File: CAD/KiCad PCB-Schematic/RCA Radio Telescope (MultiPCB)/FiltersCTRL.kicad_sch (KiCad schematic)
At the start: 12 parts, among them J11 Conn_01x04_MountingPin, U5 SN74AVC2T45DCUR, U6 MIC5365-1.8YC5-TR, U7 MIC5365-3.3YC5-TR

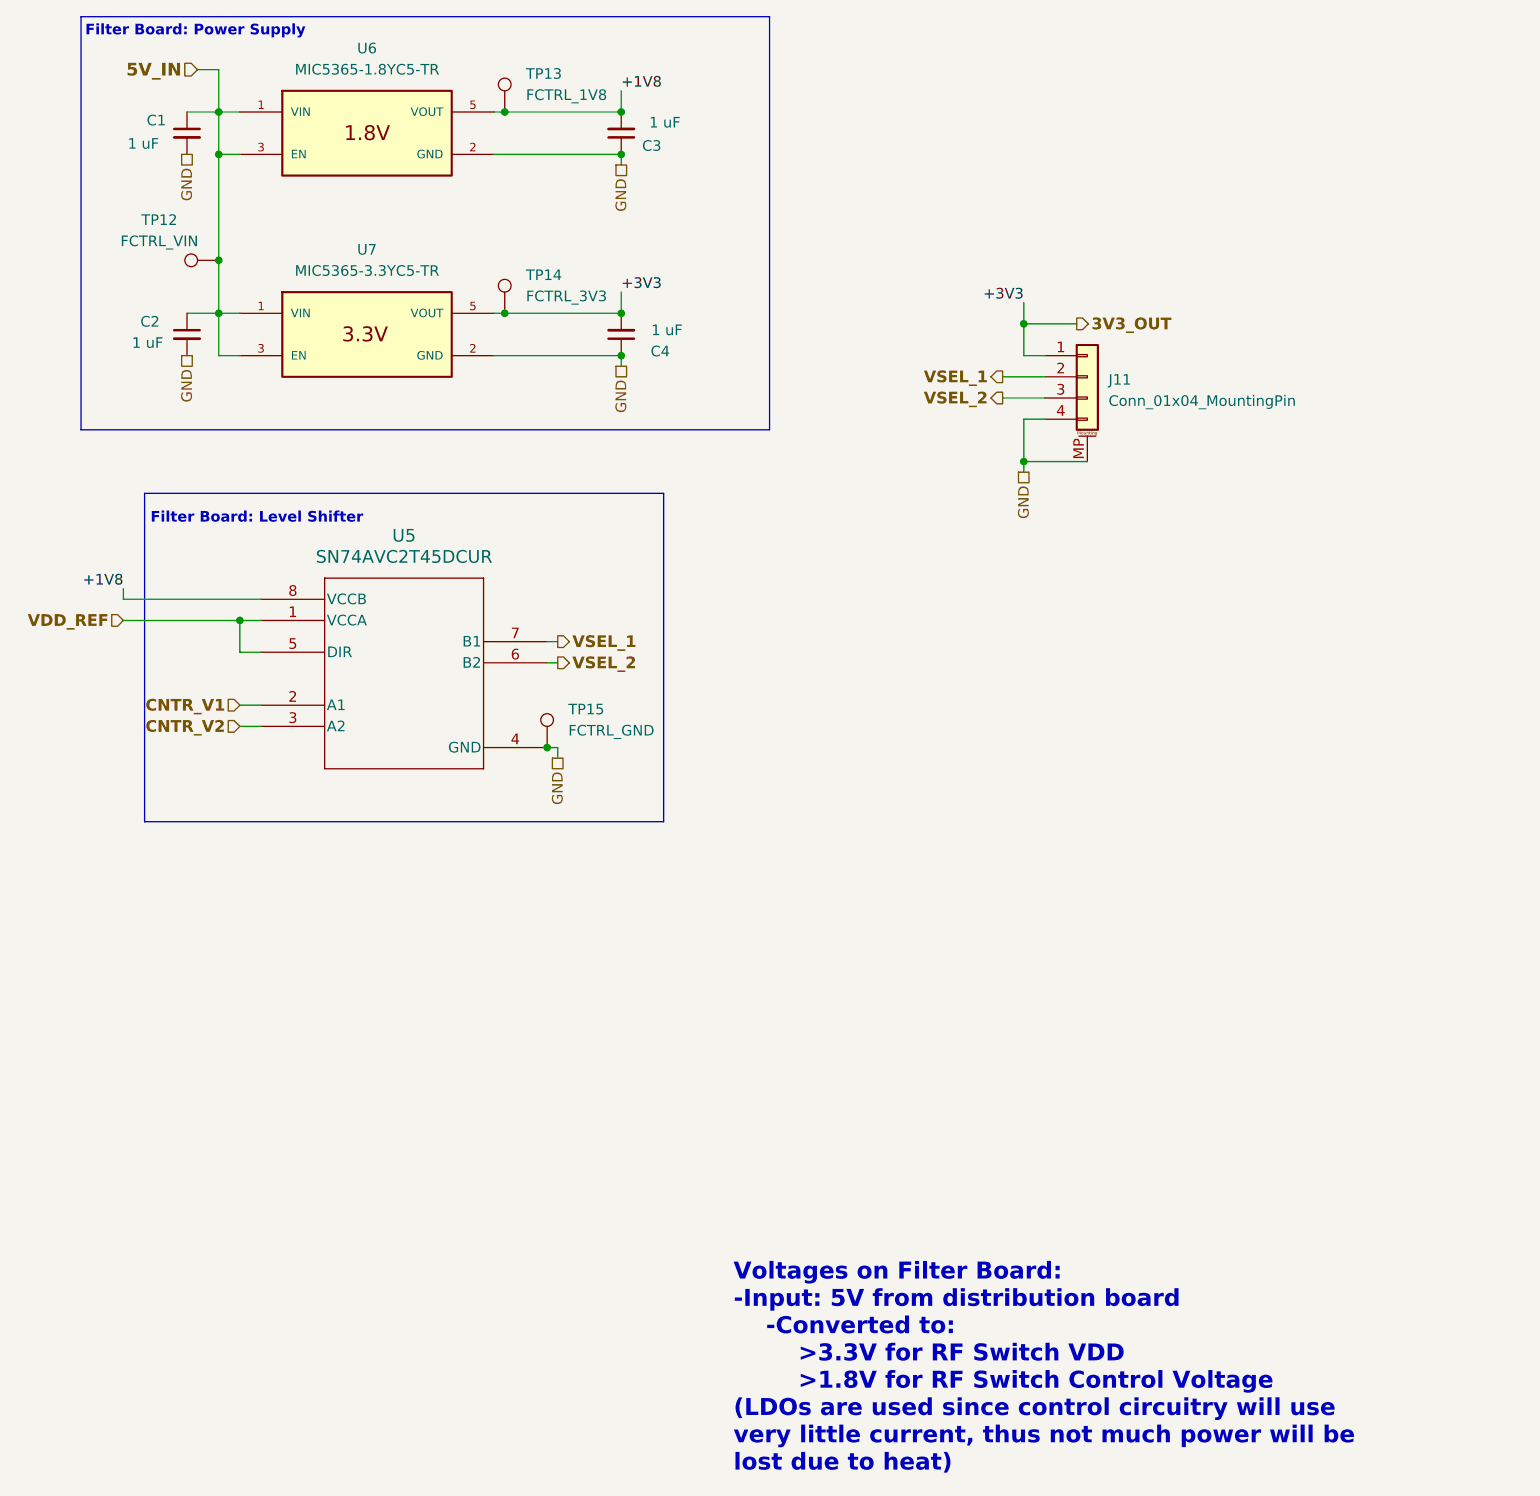
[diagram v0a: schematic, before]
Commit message: Update to Schematic and PCB
Filter Control Schematic to v1.5
- Removed redundant connector symbol

Root Schematic to v1.9
- Adjusted pin connections for J14 and J14

Created Matching Network PCB
- Filter Board Schematic renamed to MatchNetwork
- Placed RF switches, traces, holes for daughter board, and ground stitching
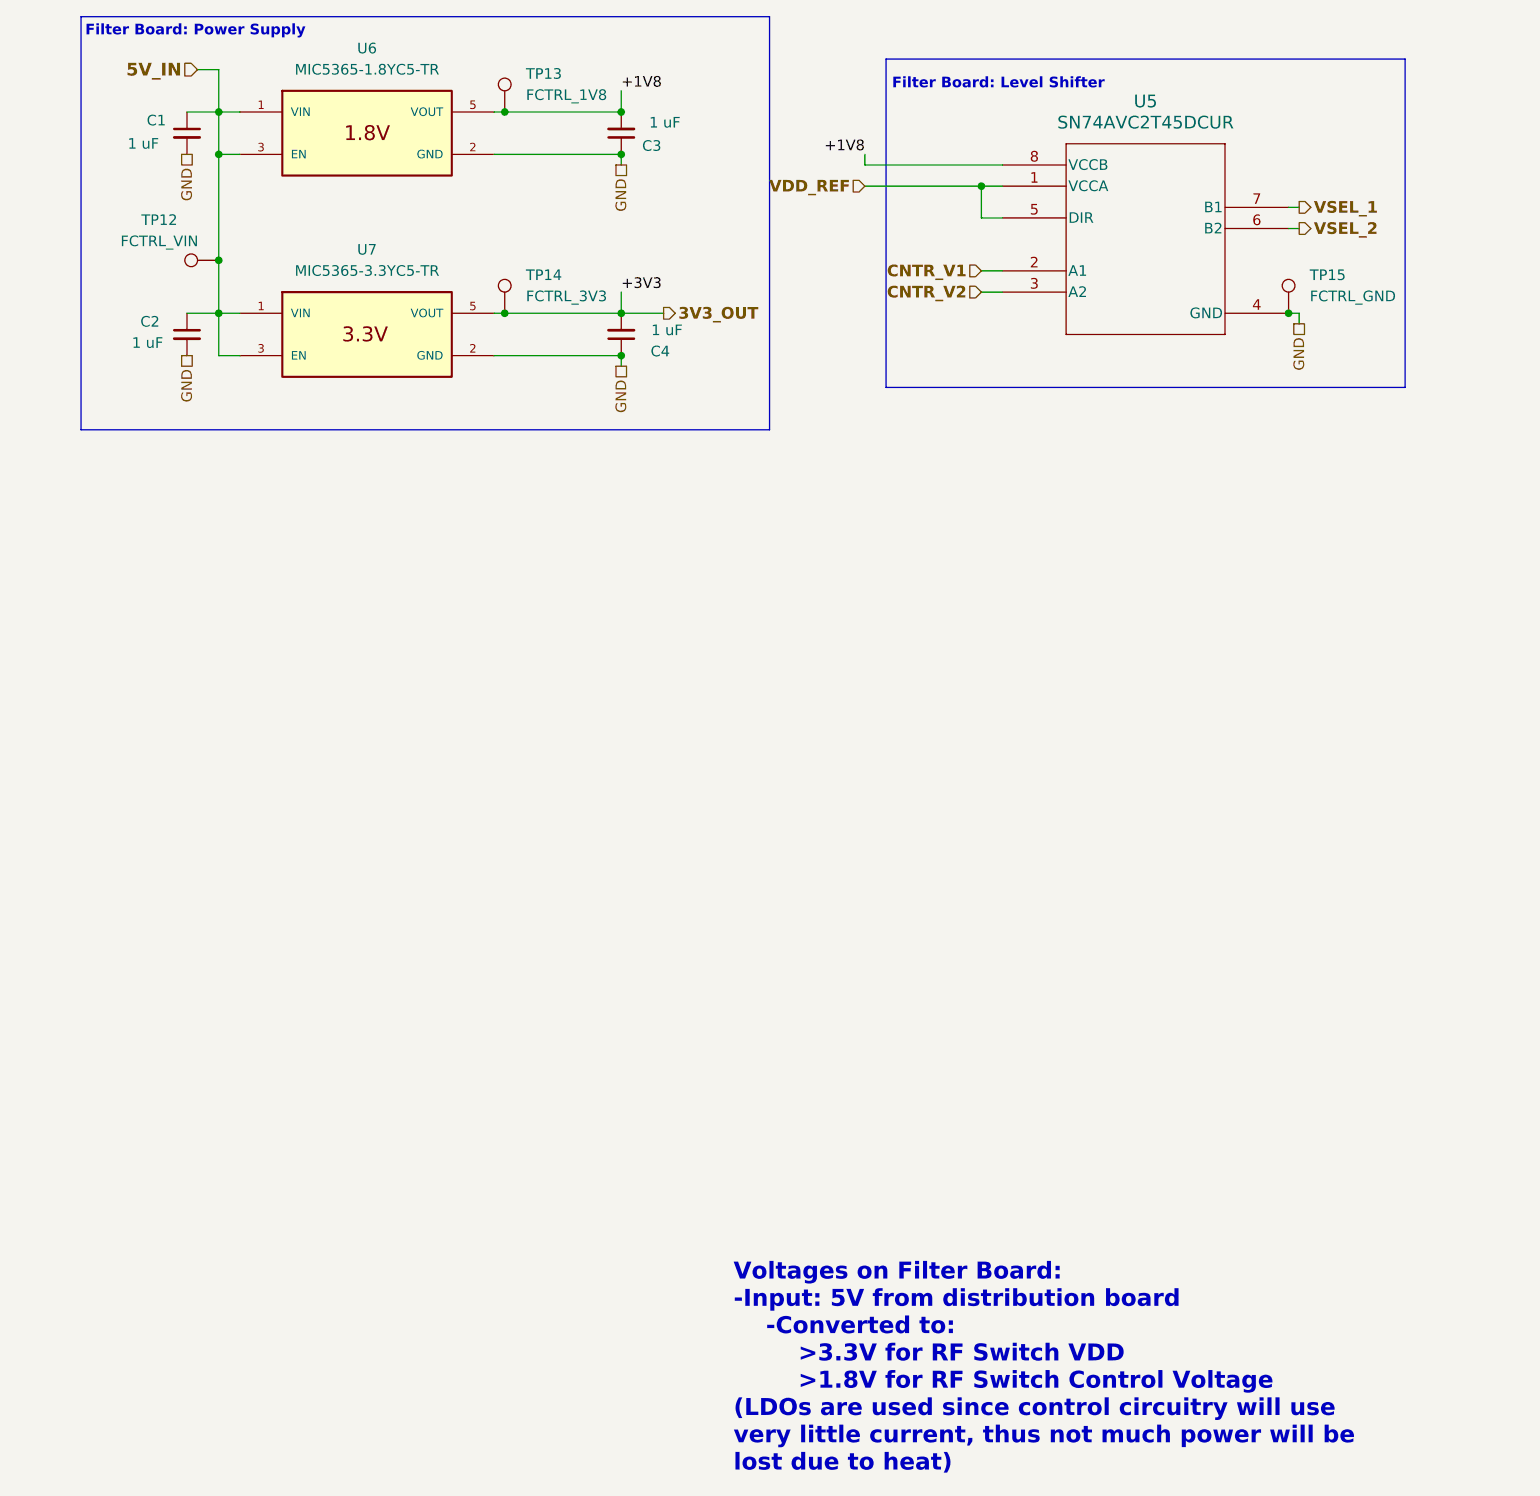
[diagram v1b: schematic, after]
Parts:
- removed J11: Conn_01x04_MountingPin, Connector_PinHeader_2.54mm:PinHeader_1x04_P2.54mm_Vertical, symbol Connector_Generic_MountingPin:Conn_01x04_MountingPin
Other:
- moved on the sheet: TP15, U5
